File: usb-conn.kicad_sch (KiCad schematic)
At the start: 8 parts, among them J1 Conn_01x04_Pin, J2 Conn_01x04_Pin, J4 Conn_01x04_Pin, J5 Conn_01x06_Pin, P1 USB_C_Plug_USB2.0, U1 SPX3819M5-L-3-3

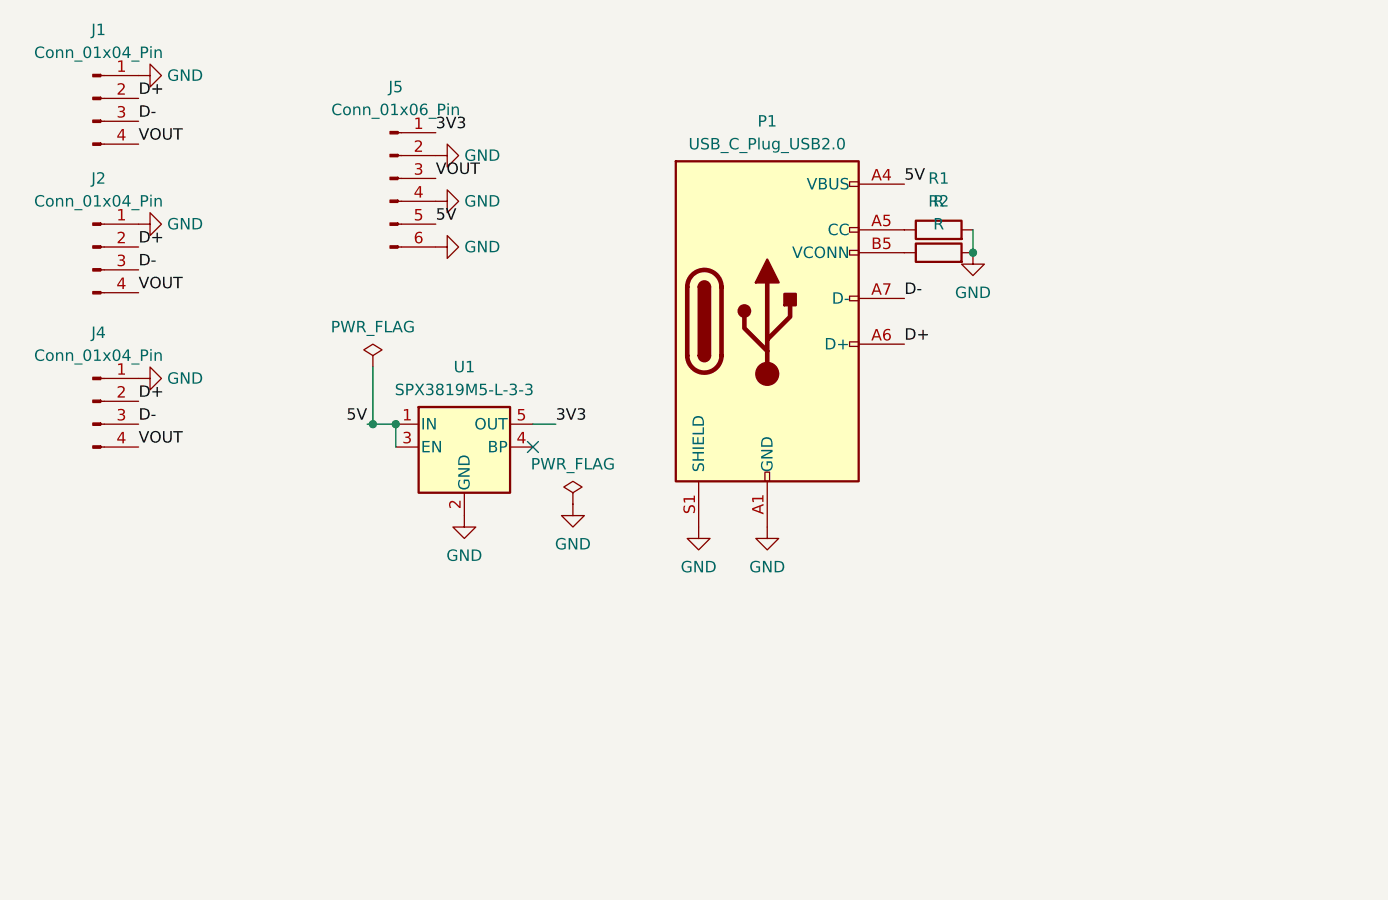
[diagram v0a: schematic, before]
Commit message: usb-conn: fix connector
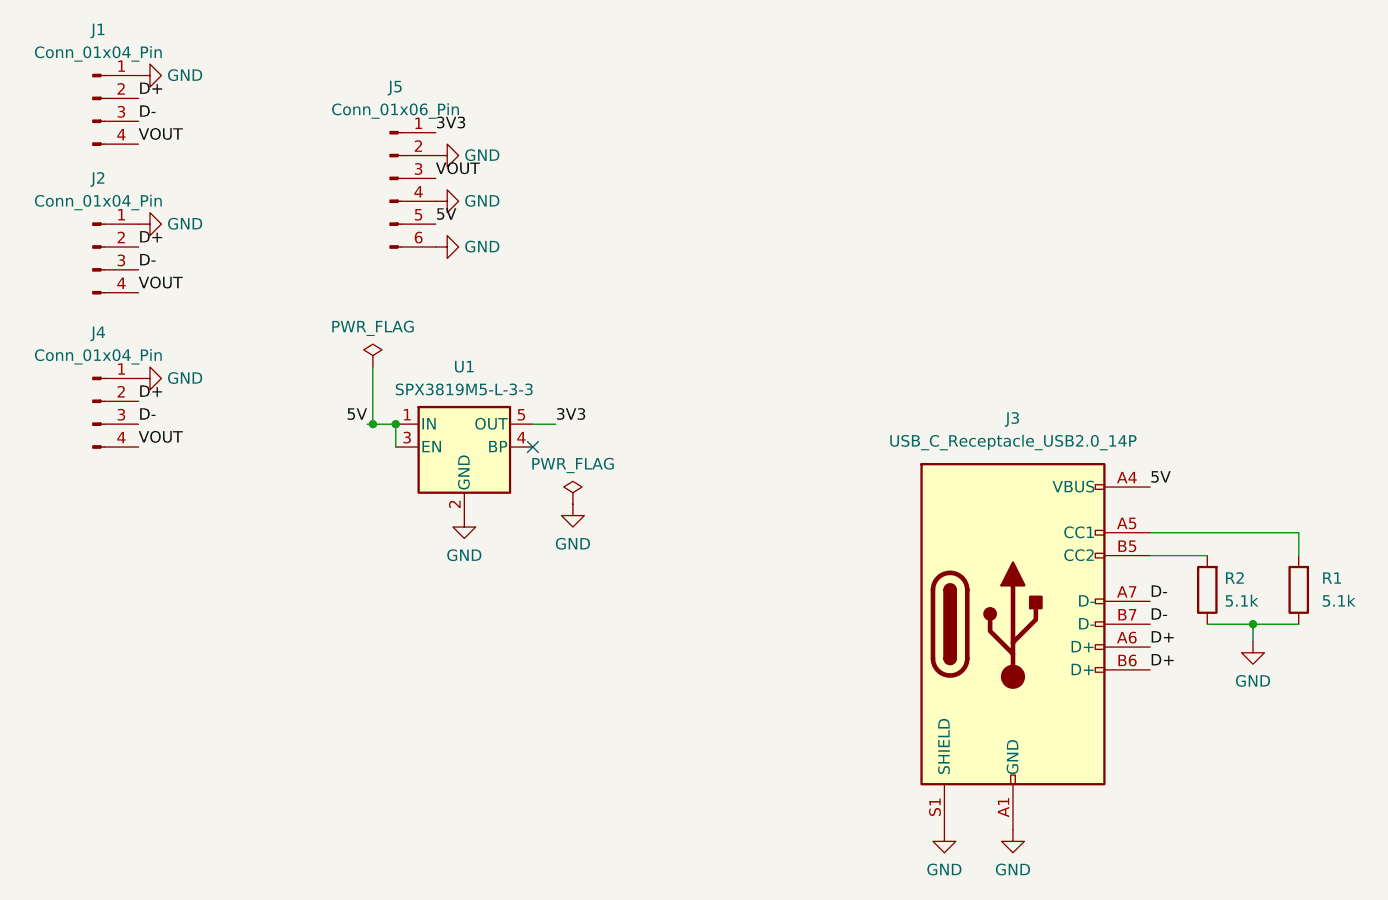
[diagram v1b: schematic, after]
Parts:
- removed P1: USB_C_Plug_USB2.0, Connector_USB:USB_C_Receptacle_XKB_U262-16XN-4BVC11, symbol Connector:USB_C_Plug_USB2.0
- added J3: USB_C_Receptacle_USB2.0_14P, Connector_USB:USB_C_Receptacle_XKB_U262-16XN-4BVC11, symbol Connector:USB_C_Receptacle_USB2.0_14P
- R1, R2: value R -> 5.1k
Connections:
- net 5V: now also J3.A4 (VBUS), J3.A9 (VBUS), J3.B4 (VBUS), J3.B9 (VBUS)
- net D+: now also J3.A6 (D+), J3.B6 (D+)
- net D-: now also J3.A7 (D-), J3.B7 (D-)
- net GND: now also R1.1, R2.1, J3.A1 (GND), J3.A12 (GND), J3.B1 (GND), J3.B12 (GND), J3.S1 (SHIELD); no longer R1.2, R2.2
- new net: J3.A5 (CC1), R1.2
- new net: J3.B5 (CC2), R2.2
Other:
- moved on the sheet: R1, R2
